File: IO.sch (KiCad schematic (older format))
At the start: 16 parts, among them U3 74AC541, U4 74LS138, U5 74HC245, U6 74LS148

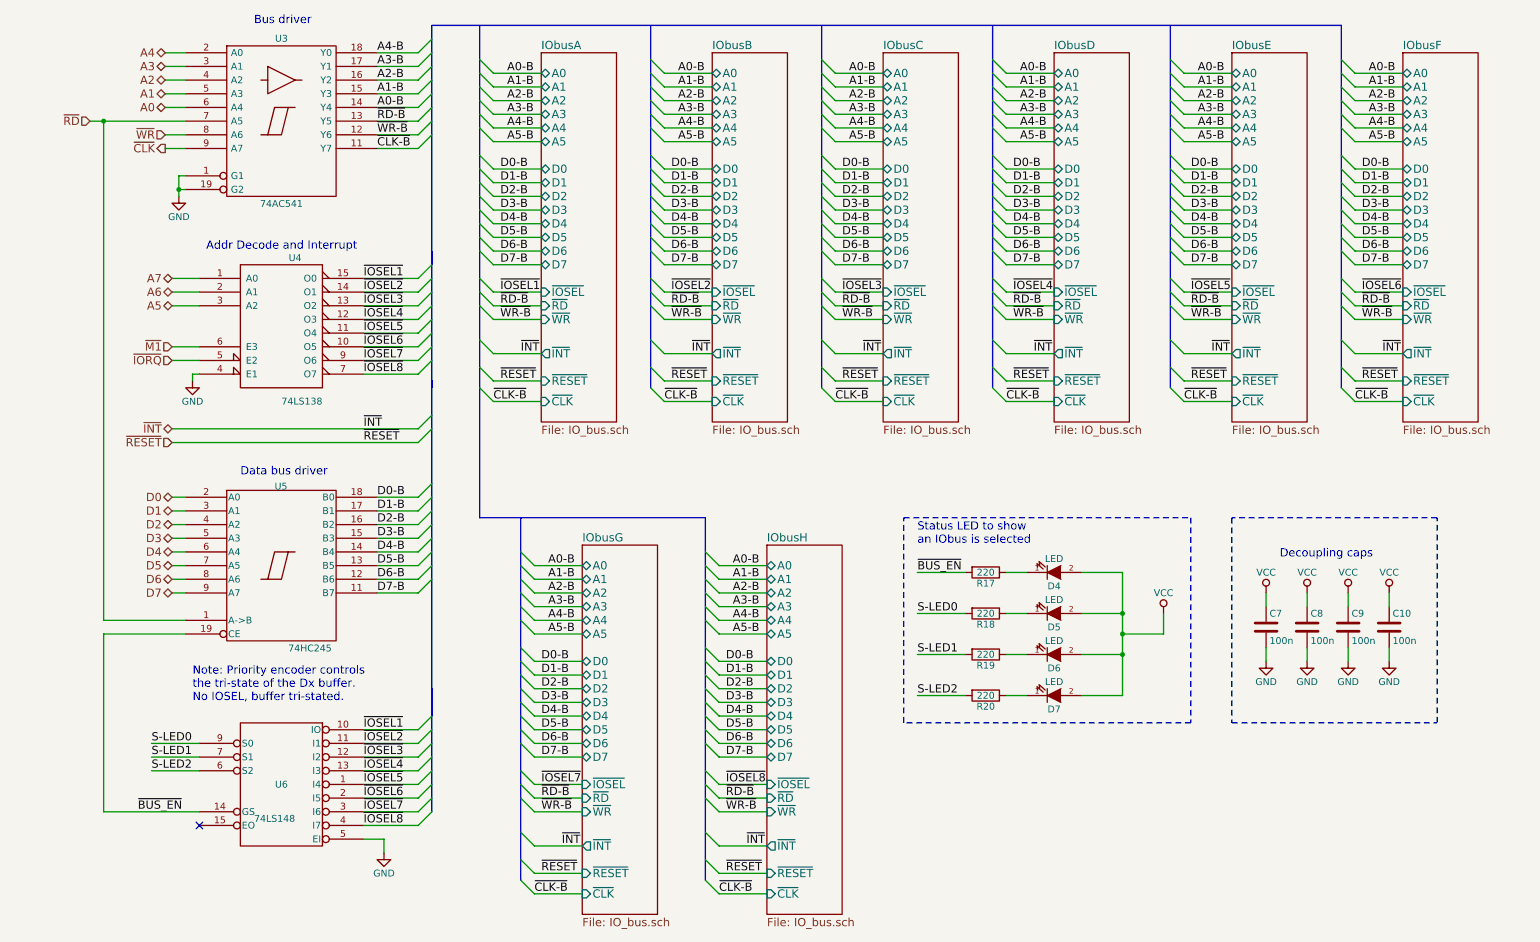
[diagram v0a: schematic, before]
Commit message: PCB layout complete, passes DRC, more tuning required
One thing not enough buffers for all address lines (missed A5), so
swapped out the CLK. Not sure if that was a good idea, but didn't want
to add another chip for a single buffer. :(
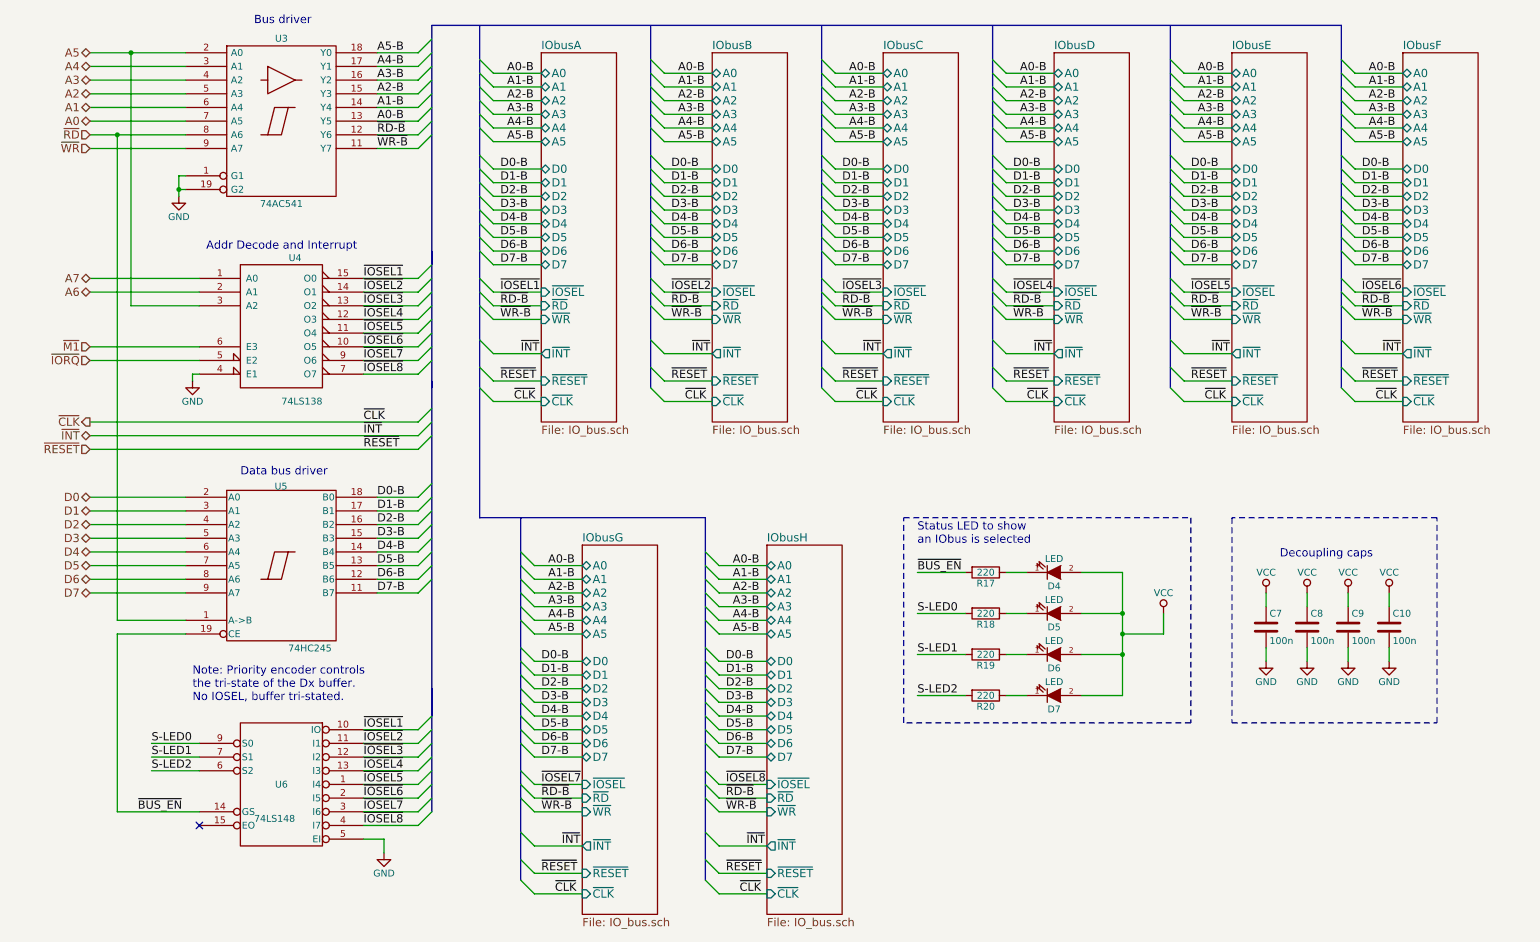
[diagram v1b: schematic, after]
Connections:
- net ~CLK-B is gone; now on net ~WR-B: U3.11 (Y7)
- net A0: now also U3.7 (A5); no longer U3.6 (A4)
- net A0-B: now also U3.13 (Y5); no longer U3.14 (Y4)
- net A1: now also U3.6 (A4); no longer U3.5 (A3)
- net A1-B: now also U3.14 (Y4); no longer U3.15 (Y3)
- net A2: now also U3.5 (A3); no longer U3.4 (A2)
- net A2-B: now also U3.15 (Y3); no longer U3.16 (Y2)
- net A3: now also U3.4 (A2); no longer U3.3 (A1)
- net A3-B: now also U3.16 (Y2); no longer U3.17 (Y1)
- net A4: now also U3.3 (A1); no longer U3.2 (A0)
- net A4-B: now also U3.17 (Y1); no longer U3.18 (Y0)
- net A5: now also U3.2 (A0)
- net A5-B: now also U3.18 (Y0)
- net ~CLK: no longer U3.9 (A7)
- net ~RD: now also U3.8 (A6); no longer U3.7 (A5)
- net ~RD-B: now also U3.12 (Y6); no longer U3.13 (Y5)
- net ~WR: now also U3.9 (A7); no longer U3.8 (A6)
- net ~WR-B: no longer U3.12 (Y6)

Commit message: Update with smaller board and through-hole parts.
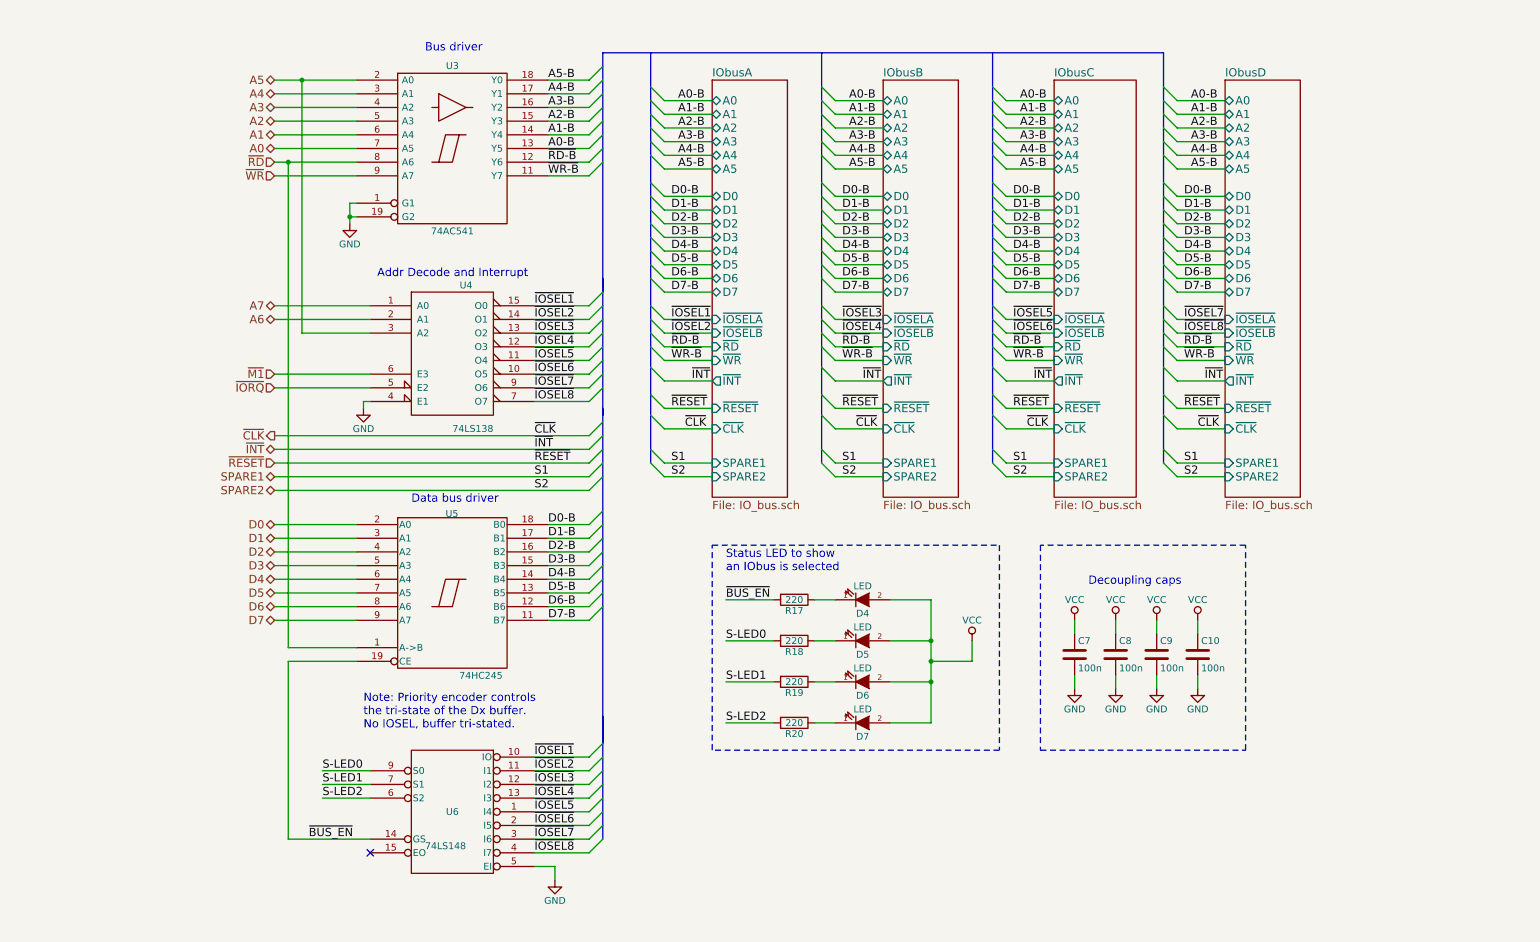
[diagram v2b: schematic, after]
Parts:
- C10, C7, C8, C9: footprint Capacitors_SMD:C_0805_HandSoldering -> Capacitors_ThroughHole:C_Rect_L4_W2.5_P2.5
- D4, D5, D6, D7: footprint LEDs:LED_1206 -> LEDs:LED-3MM
- R17, R18, R19, R20: footprint Resistors_SMD:R_0805_HandSoldering -> Resistors_ThroughHole:Resistor_Horizontal_RM7mm
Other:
- moved on the sheet: C10, C7, C8, C9, D4, D5, D6, D7, R17, R18, R19, R20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
